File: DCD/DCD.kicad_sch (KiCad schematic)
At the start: 0 parts

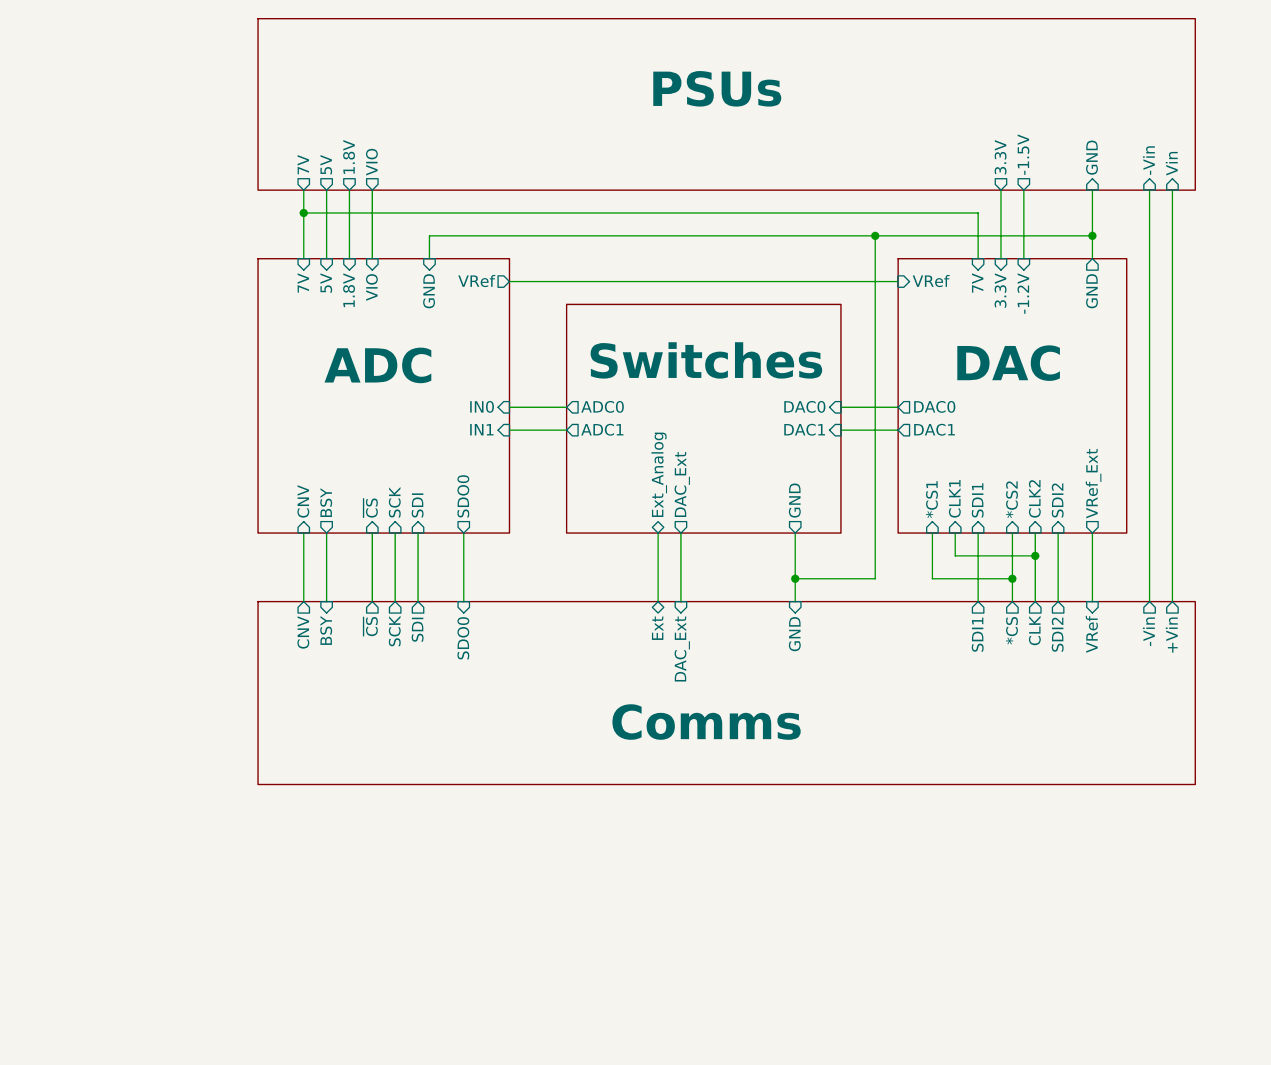
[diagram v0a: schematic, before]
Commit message: Progress on fixing the remaining footprints and 3 models
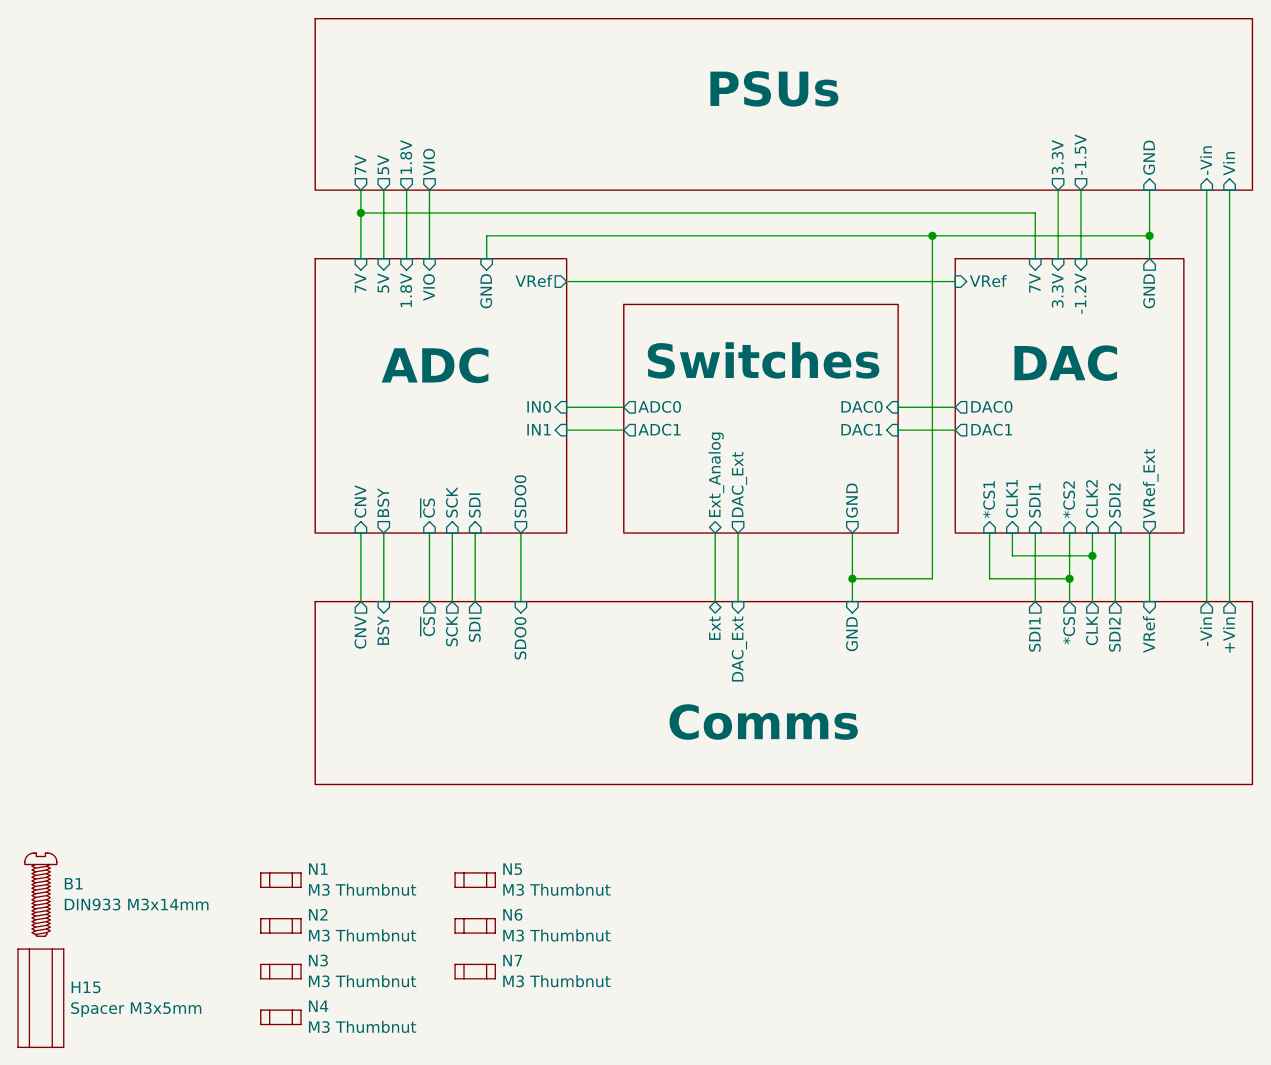
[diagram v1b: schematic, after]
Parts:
- added B1: DIN933 M3x14mm, LOBSTER:Screw_DIN933_M3x14mm, symbol LOBSTER:Bolt_M2x8mm
- added H15: Spacer M3x5mm, LOBSTER:ThreadedSpacer_6mm_M3x0.5_5mm, symbol DreamCrusher-breakout-internal-rescue:ThreadedSpacer_Short-LOBSTER
- added N1, N2, N3, N4, N5, N6, N7: M3 Thumbnut, LOBSTER:ThumbNut-M3, symbol LOBSTER:Nut_M2

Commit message: Progress on the layout
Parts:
- B1: footprint LOBSTER:Screw_DIN933_M3x14mm -> custom_components:Screw_DIN933_M3x14mm
- H15: footprint LOBSTER:ThreadedSpacer_6mm_M3x0.5_5mm -> custom_components:ThreadedSpacer_6mm_M3x0.5_5mm
- N1, N2, N3, N4, N5, N6, N7: footprint LOBSTER:ThumbNut-M3 -> custom_components:ThumbNut-M3
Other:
- sheet ADC ports: added AGND, DGND; removed GND
- sheet Comms ports: added AGND, DGND; removed GND
- sheet DAC ports: added AGND, DGND; removed GND
- sheet PSUs ports: added -1.8V; removed -1.5V
- sheet Switches ports: added AGND; removed GND

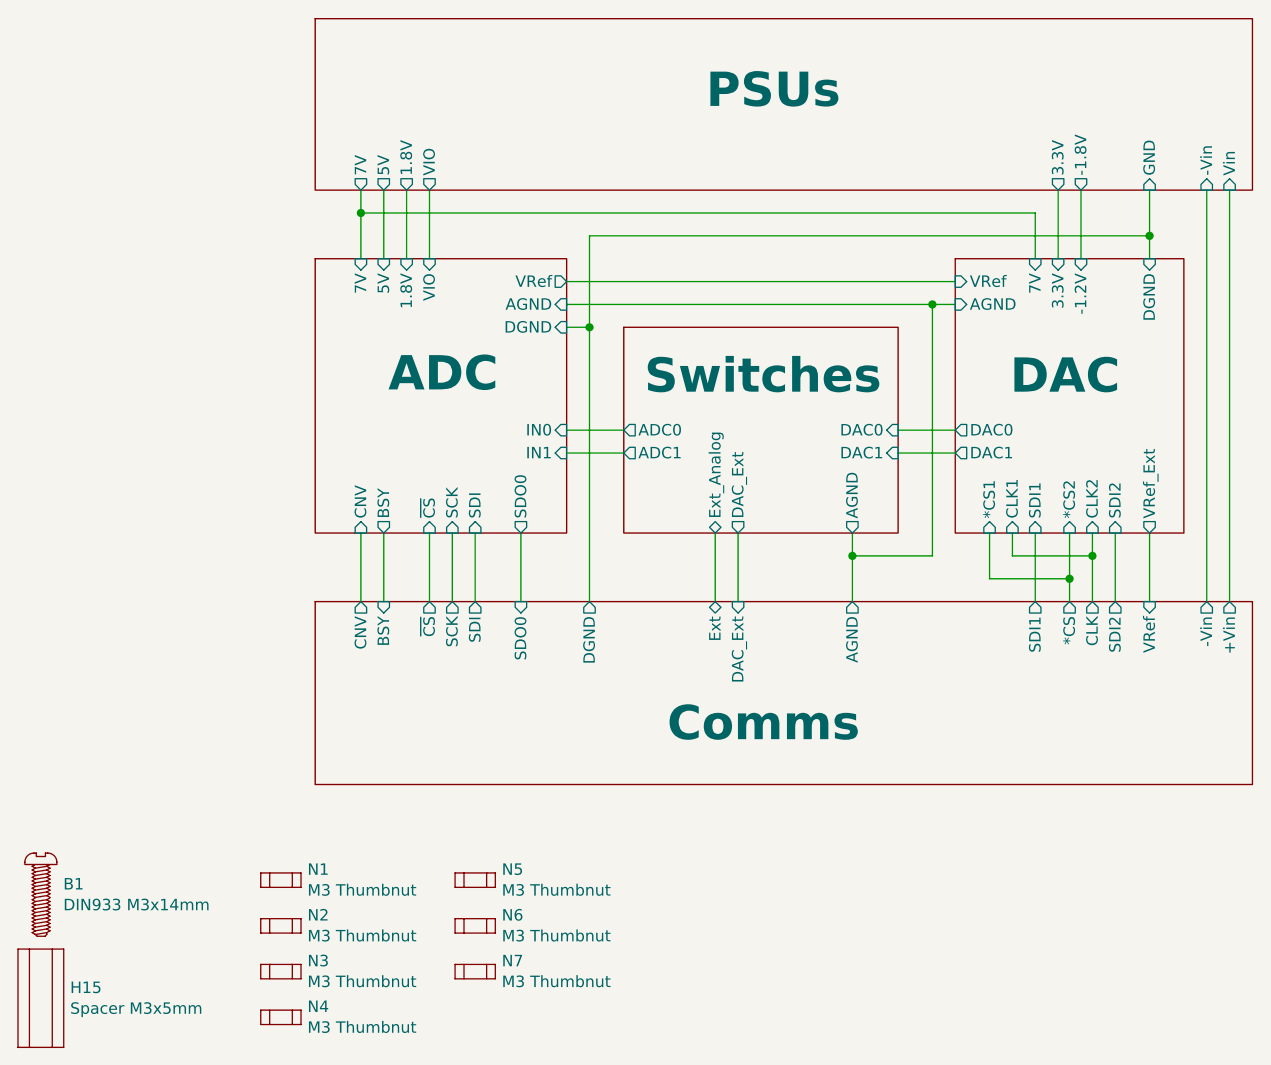
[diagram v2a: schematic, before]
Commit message: Schematics for the clock reconditioning
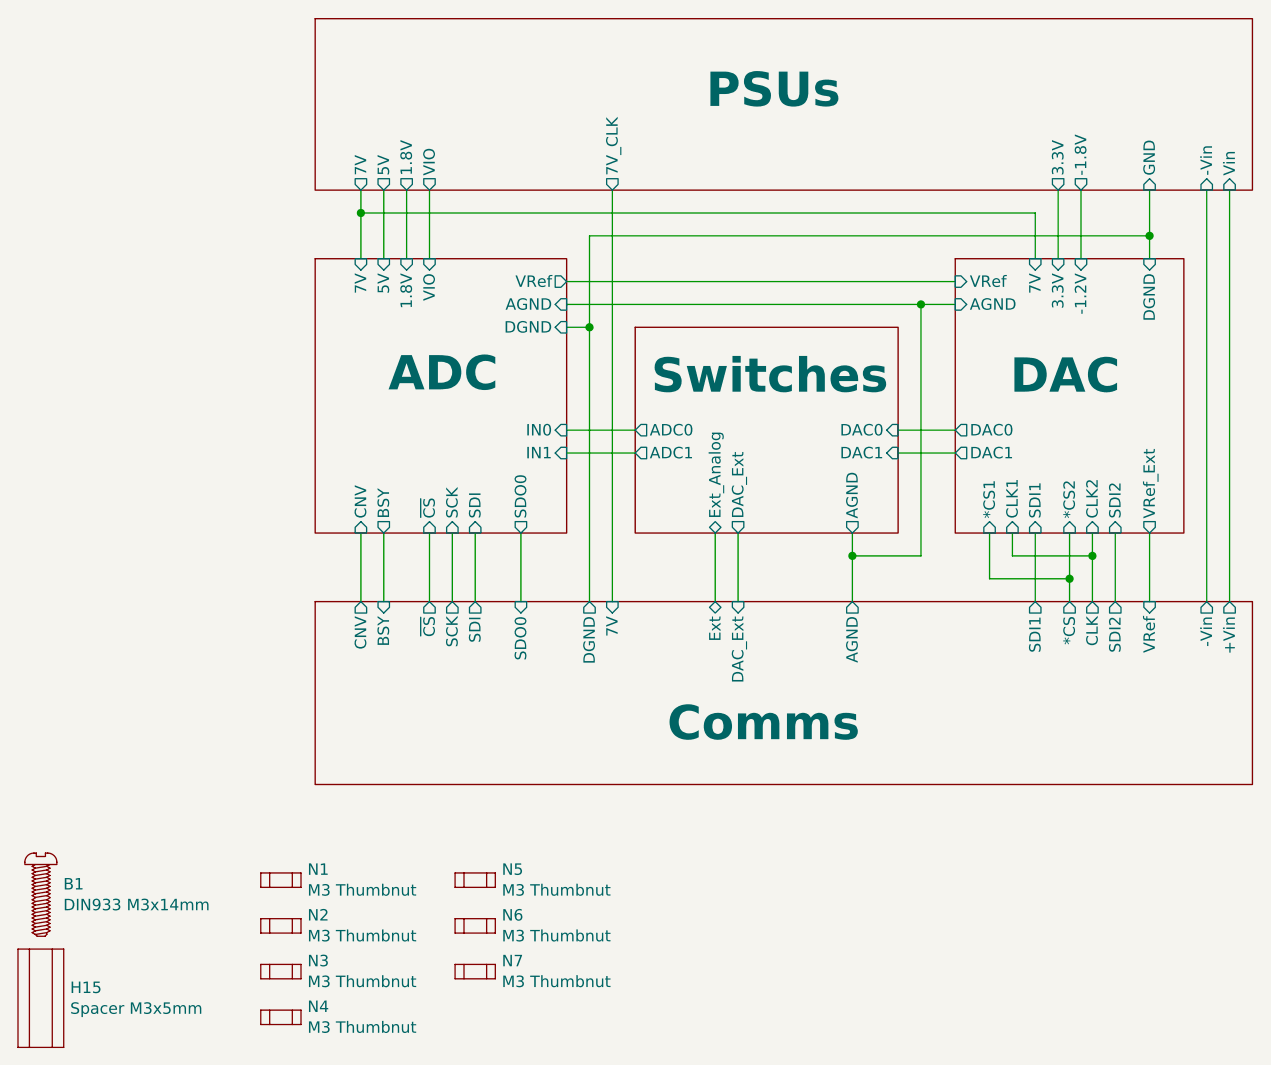
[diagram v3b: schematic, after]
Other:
- sheet Comms ports: added 7V; removed none
- sheet PSUs ports: added 7V_CLK; removed none
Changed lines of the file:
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@@
+	)
+	(junction
+		(at 119.38 46.99)
+		(diameter 0)
+		(color 0 0 0 0)
 	)
 	(junction
@@
 		(color 0 0 0 0)
 	)
-	(junction
-		(at 120.65 46.99)
-		(diameter 0)
-		(color 0 0 0 0)
-	)
-	(wire
-		(pts
-			(xy 120.65 46.99) (xy 120.65 74.93)
+	(wire
+		(pts
+			(xy 119.38 46.99) (xy 119.38 74.93)
 		)
 		(stroke
@@
 	(wire
 		(pts
-			(xy 111.76 74.93) (xy 120.65 74.93)
+			(xy 111.76 74.93) (xy 119.38 74.93)
 		)
 		(stroke
@@
 	(wire
 		(pts
-			(xy 80.01 63.5) (xy 86.36 63.5)
+			(xy 80.01 63.5) (xy 87.63 63.5)
 		)
 		(stroke
@@
 	(wire
 		(pts
-			(xy 80.01 46.99) (xy 120.65 46.99)
+			(xy 80.01 46.99) (xy 119.38 46.99)
 		)
 		(stroke
@@
 	(wire
 		(pts
-			(xy 123.19 46.99) (xy 120.65 46.99)
+			(xy 85.09 34.29) (xy 85.09 80.01)
 		)
 		(stroke
@@
 	(wire
 		(pts
-			(xy 80.01 60.96) (xy 86.36 60.96)
+			(xy 80.01 60.96) (xy 87.63 60.96)
 		)
 		(stroke
@@
 		(pts
 			(xy 57.15 34.29) (xy 57.15 36.83)
+		)
+		(stroke
+			(width 0)
+			(type default)
+		)
+	)
+	(wire
+		(pts
+			(xy 119.38 46.99) (xy 123.19 46.99)
 		)
 		(stroke
@@
 			)
 		)
+		(pin "7V" input
+			(at 85.09 80.01 90)
+			(effects
+				(font
+					(size 1.27 1.27)
+				)
+				(justify right)
+			)
+		)
 		(instances
 			(project "DCD"
@@
 			)
 		)
+		(pin "7V_CLK" output
+			(at 85.09 34.29 270)
+			(effects
+				(font
+					(size 1.27 1.27)
+				)
+				(justify left)
+			)
+		)
 		(instances
 			(project "DCD"
@@
 	)
 	(sheet
-		(at 86.36 49.53)
-		(size 30.48 22.86)
+		(at 87.63 49.53)
+		(size 29.21 22.86)
 		(exclude_from_sim no)
 		(in_bom yes)
@@
 		)
 		(property "Sheetname" "Switches"
-			(at 88.646 57.15 0)
+			(at 89.408 57.15 0)
 			(effects
 				(font
@@
 		)
 		(property "Sheetfile" "Subcircuits/switches.kicad_sch"
-			(at 86.36 80.5946 0)
+			(at 87.63 80.5946 0)
 			(effects
 				(font
@@
 		)
 		(pin "ADC0" output
-			(at 86.36 60.96 180)
+			(at 87.63 60.96 180)
 			(effects
 				(font
@@
 		)
 		(pin "ADC1" output
-			(at 86.36 63.5 180)
-			(effects
-				(font
+			(at 87.63 63.5 180)
+			(effects
+				(font

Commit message: Layout mostly done
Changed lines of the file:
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@@
 	(paper "A5")
 	(junction
-		(at 135.89 77.47)
-		(diameter 0)
-		(color 0 0 0 0)
-	)
-	(junction
 		(at 111.76 74.93)
 		(diameter 0)
@@
 	)
 	(junction
-		(at 138.43 74.93)
-		(diameter 0)
-		(color 0 0 0 0)
-	)
-	(junction
 		(at 57.15 36.83)
 		(diameter 0)
@@
 	(wire
 		(pts
-			(xy 129.54 74.93) (xy 138.43 74.93)
-		)
-		(stroke
-			(width 0)
-			(type default)
-		)
-	)
-	(wire
-		(pts
 			(xy 116.84 60.96) (xy 123.19 60.96)
 		)
@@
 	(wire
 		(pts
-			(xy 138.43 74.93) (xy 138.43 80.01)
+			(xy 138.43 72.39) (xy 138.43 80.01)
 		)
 		(stroke
@@
 	(wire
 		(pts
-			(xy 135.89 72.39) (xy 135.89 77.47)
-		)
-		(stroke
-			(width 0)
-			(type default)
-		)
-	)
-	(wire
-		(pts
 			(xy 132.08 41.91) (xy 132.08 36.83)
 		)
@@
 	(wire
 		(pts
-			(xy 135.89 77.47) (xy 127 77.47)
-		)
-		(stroke
-			(width 0)
-			(type default)
-		)
-	)
-	(wire
-		(pts
 			(xy 140.97 72.39) (xy 140.97 80.01)
 		)
@@
 	(wire
 		(pts
-			(xy 138.43 72.39) (xy 138.43 74.93)
-		)
-		(stroke
-			(width 0)
-			(type default)
-		)
-	)
-	(wire
-		(pts
 			(xy 144.78 34.29) (xy 144.78 39.37)
 		)
@@
 	(wire
 		(pts
-			(xy 135.89 77.47) (xy 135.89 80.01)
-		)
-		(stroke
+			(xy 135.89 72.39) (xy 135.89 80.01)
+		)
+		(stroke

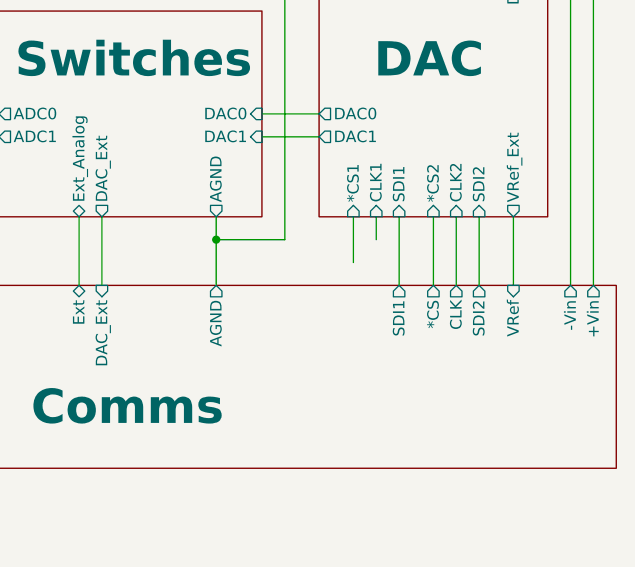
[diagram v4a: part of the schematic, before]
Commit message: Connected the pin header in the schematics
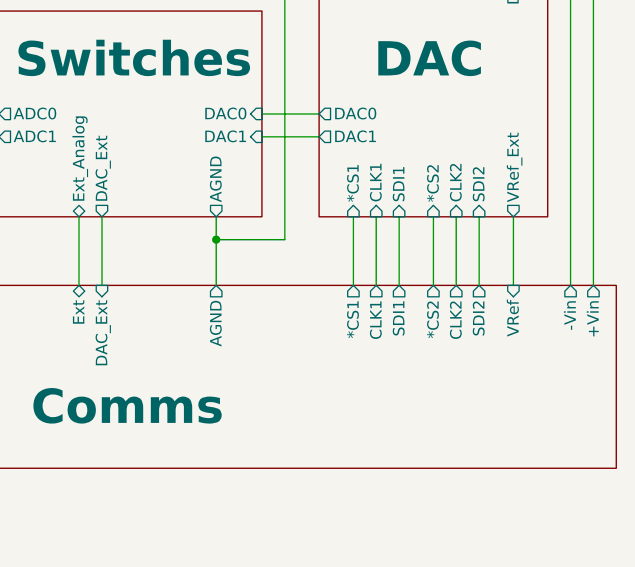
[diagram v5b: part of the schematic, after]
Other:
- sheet Comms ports: added *CS1, *CS2, CLK1, CLK2; removed *CS, CLK
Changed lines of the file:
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@@
 	(wire
 		(pts
-			(xy 127 77.47) (xy 127 72.39)
+			(xy 127 72.39) (xy 127 80.01)
 		)
 		(stroke
@@
 	(wire
 		(pts
-			(xy 129.54 72.39) (xy 129.54 74.93)
+			(xy 129.54 72.39) (xy 129.54 80.01)
 		)
 		(stroke
@@
 			)
 		)
-		(pin "CLK" output
-			(at 138.43 80.01 90)
-			(effects
-				(font
-					(size 1.27 1.27)
-				)
-				(justify right)
-			)
-		)
 		(pin "VRef" input
 			(at 144.78 80.01 90)
@@
 			)
 		)
-		(pin "*CS" output
-			(at 135.89 80.01 90)
-			(effects
-				(font
-					(size 1.27 1.27)
-				)
-				(justify right)
-			)
-		)
 		(pin "+Vin" output
 			(at 153.67 80.01 90)
@@
 			(effects
 				(font
+					(size 1.27 1.27)
+				)
+				(justify right)
+			)
+		)
+		(pin "CLK1" output
+			(at 129.54 80.01 90)
+			(effects
+				(font
+					(size 1.27 1.27)
+				)
+				(justify right)
+			)
+		)
+		(pin "*CS2" output
+			(at 135.89 80.01 90)
+			(effects
+				(font
+					(size 1.27 1.27)
+				)
+				(justify right)
+			)
+		)
+		(pin "CLK2" output
+			(at 138.43 80.01 90)
+			(effects
+				(font
+					(size 1.27 1.27)
+				)
+				(justify right)
+			)
+		)
+		(pin "*CS1" output
+			(at 127 80.01 90)
+			(effects
+				(font
